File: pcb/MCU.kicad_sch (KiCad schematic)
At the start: 48 parts, among them J3 Conn_ST_STDC14, J4 Micro_SD_Card, SW1 SW_BLUE, SW2 SW_BLACK, U7 STM32U595ZJTx, Y2 16MHz

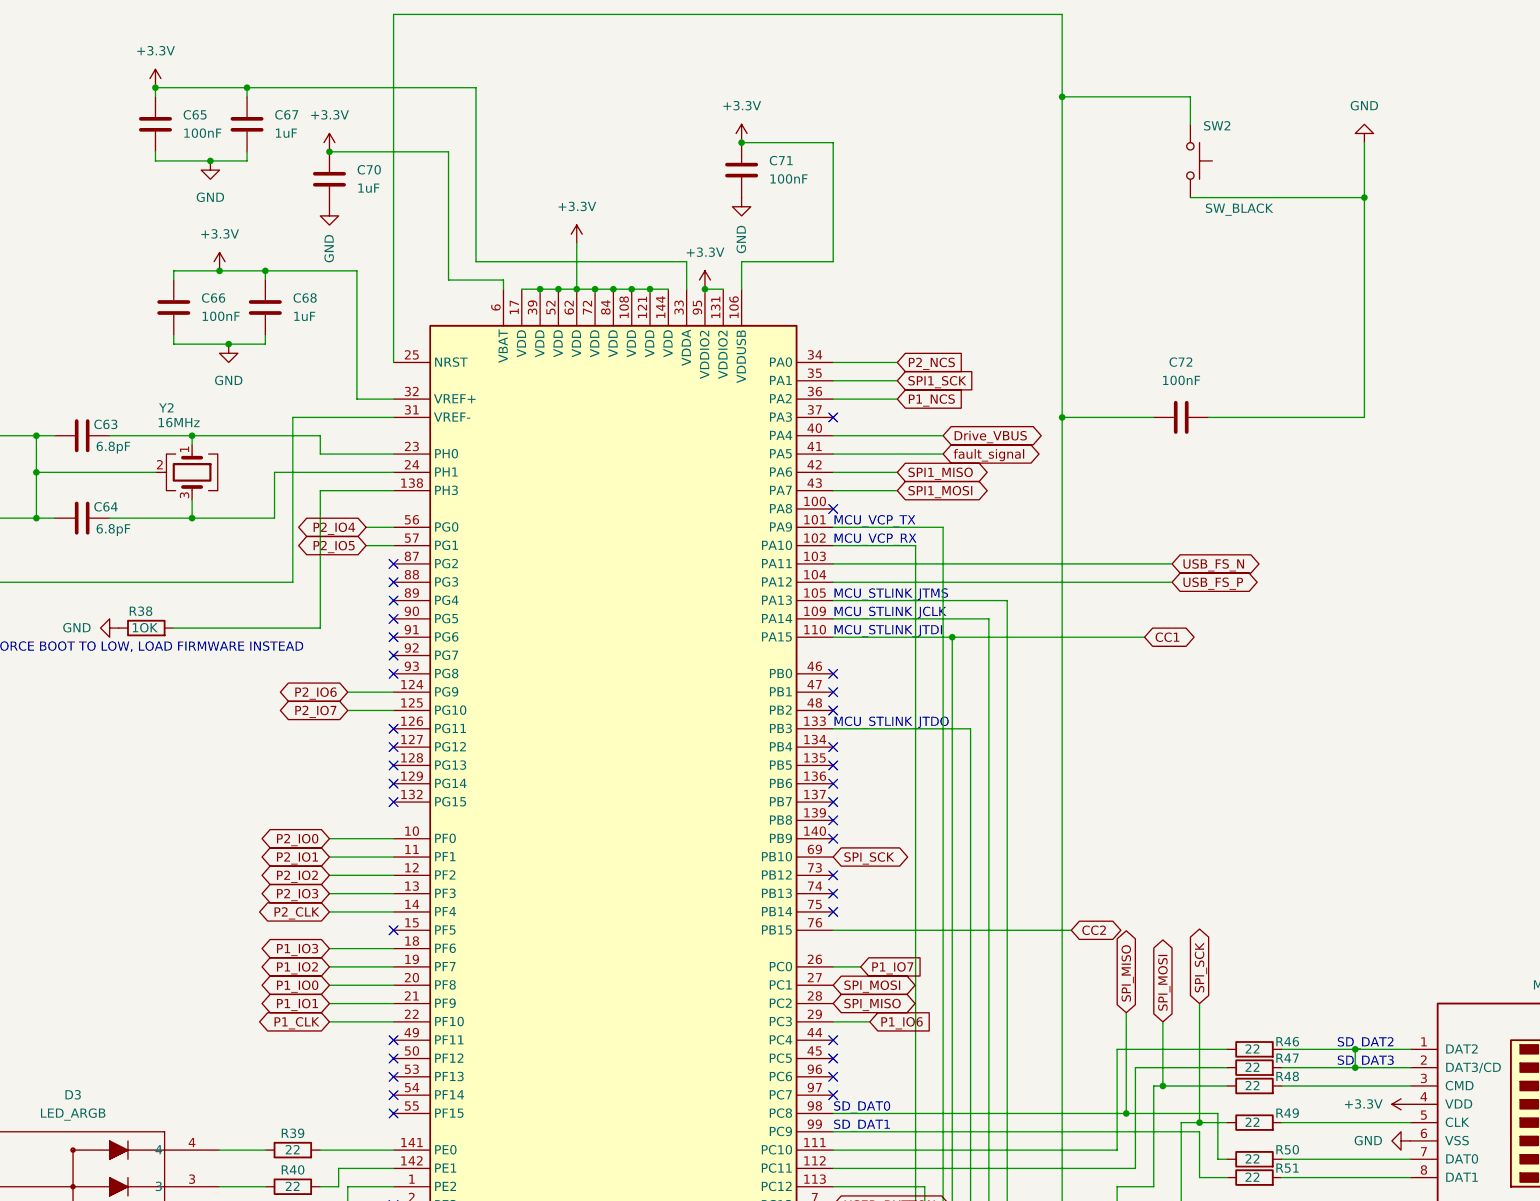
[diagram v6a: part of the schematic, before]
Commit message: pcb: mcu, sd card, jtag layout
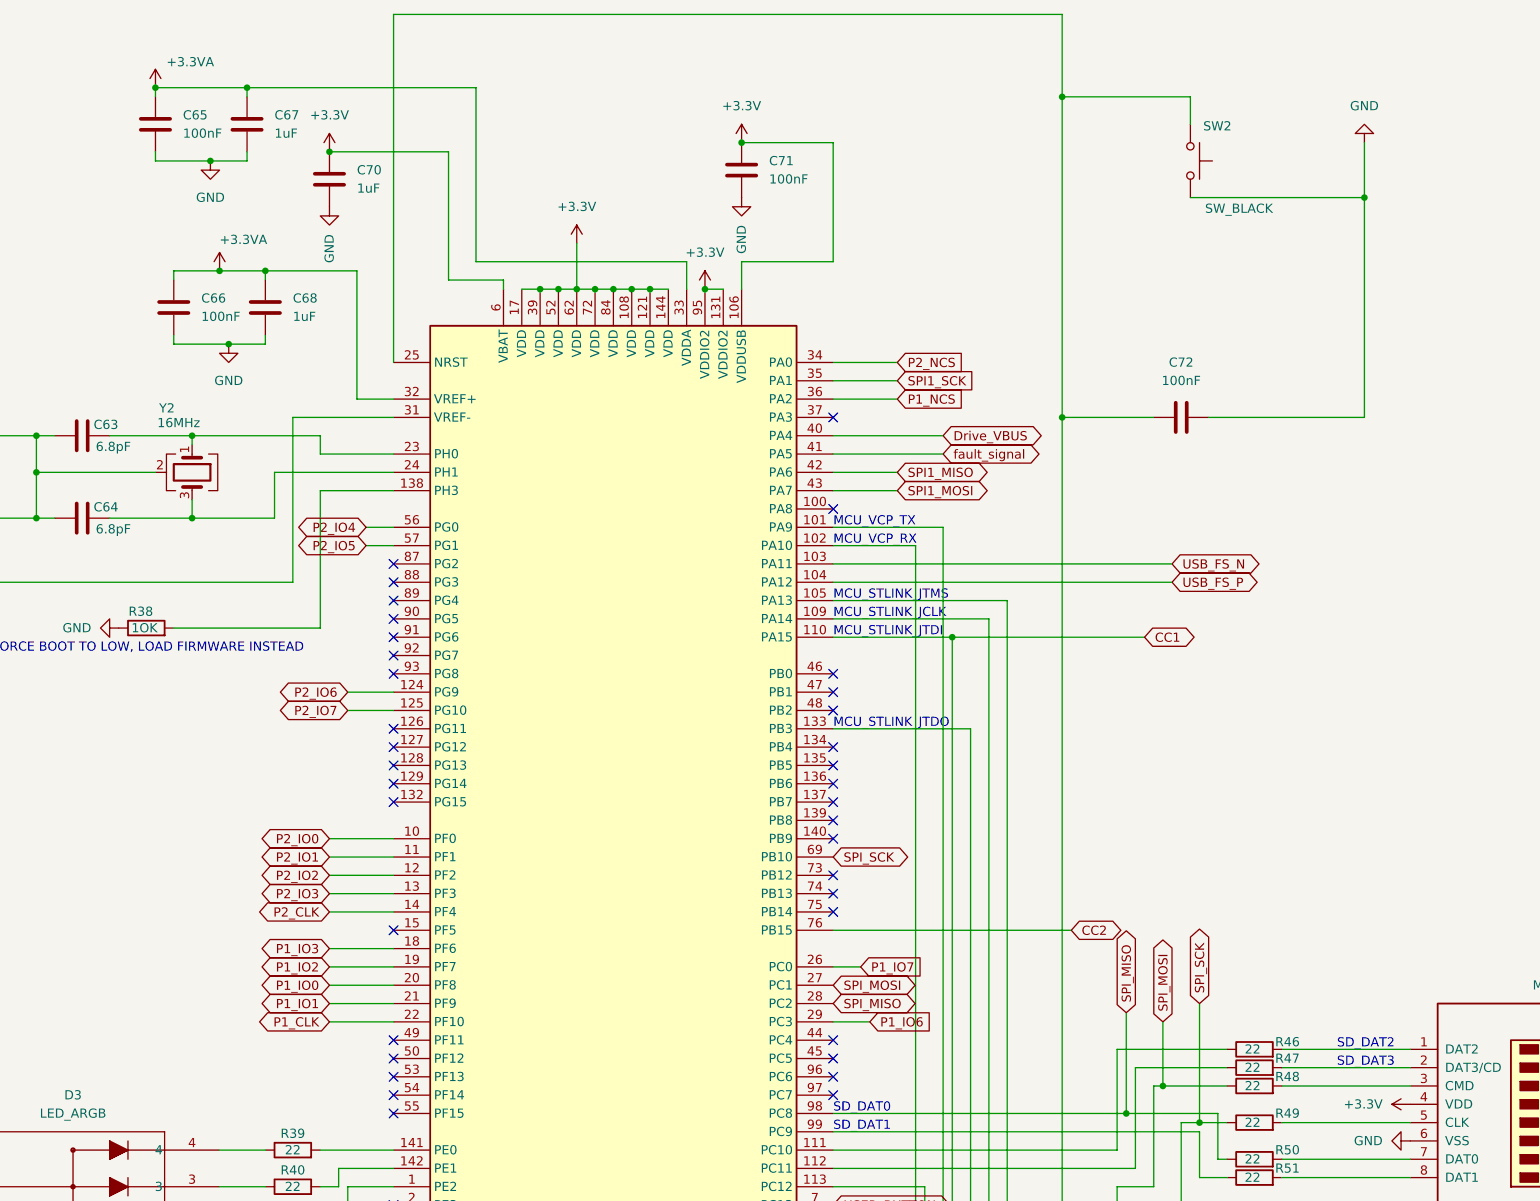
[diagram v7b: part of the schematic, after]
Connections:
- net +3.3V: no longer C65.1, C66.1, C67.1, C68.1, U7.32 (VREF+), U7.33 (VDDA)
- net at J4.1 (DAT2), R46.2: no longer J4.2 (DAT3/CD), R47.2
- new net: J4.2 (DAT3/CD), R47.2
- new net +3.3VA: C65.1, C66.1, C67.1, C68.1, U7.32 (VREF+), U7.33 (VDDA)
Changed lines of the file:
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@@
 	)
 	(junction
-		(at 289.56 166.37)
-		(diameter 0)
-		(color 0 0 0 0)
-	)
-	(junction
 		(at 320.04 217.17)
 		(diameter 0)
@@
 	)
 	(junction
-		(at 289.56 163.83)
-		(diameter 0)
-		(color 0 0 0 0)
-	)
-	(junction
 		(at 35.56 166.37)
 		(diameter 0)
@@
 	(wire
 		(pts
-			(xy 289.56 163.83) (xy 297.18 163.83)
+			(xy 279.4 163.83) (xy 297.18 163.83)
 		)
 		(stroke
@@
 	(wire
 		(pts
-			(xy 279.4 163.83) (xy 289.56 163.83)
-		)
-		(stroke
-			(width 0)
-			(type default)
-		)
-	)
-	(wire
-		(pts
 			(xy 139.7 220.98) (xy 139.7 224.79)
 		)
@@
 	(wire
 		(pts
-			(xy 289.56 163.83) (xy 289.56 166.37)
-		)
-		(stroke
-			(width 0)
-			(type default)
-		)
-	)
-	(wire
-		(pts
 			(xy 142.24 99.06) (xy 78.74 99.06)
 		)
@@
 		(in_pos_files yes)
 		(dnp no)
-		(fields_autoplaced yes)
 		(property "Reference" "#PWR056"
 			(at 132.08 59.69 0)
@@
 			)
 		)
-		(property "Value" "+3.3V"
-			(at 132.08 50.8 0)
+		(property "Value" "+3.3VA"
+			(at 132.08 51.562 0)
 			(show_name no)
 			(do_not_autoplace no)
@@
 					(size 1.27 1.27)
 				)
+				(justify left)
 			)
 		)
@@
 		(in_pos_files yes)
 		(dnp no)
-		(fields_autoplaced yes)
 		(property "Reference" "#PWR054"
 			(at 123.19 34.29 0)
@@
 			)
 		)
-		(property "Value" "+3.3V"
-			(at 123.19 25.4 0)
+		(property "Value" "+3.3VA"
+			(at 124.714 26.924 0)
 			(show_name no)
 			(do_not_autoplace no)
@@
 					(size 1.27 1.27)
 				)
+				(justify left)
 			)
 		)

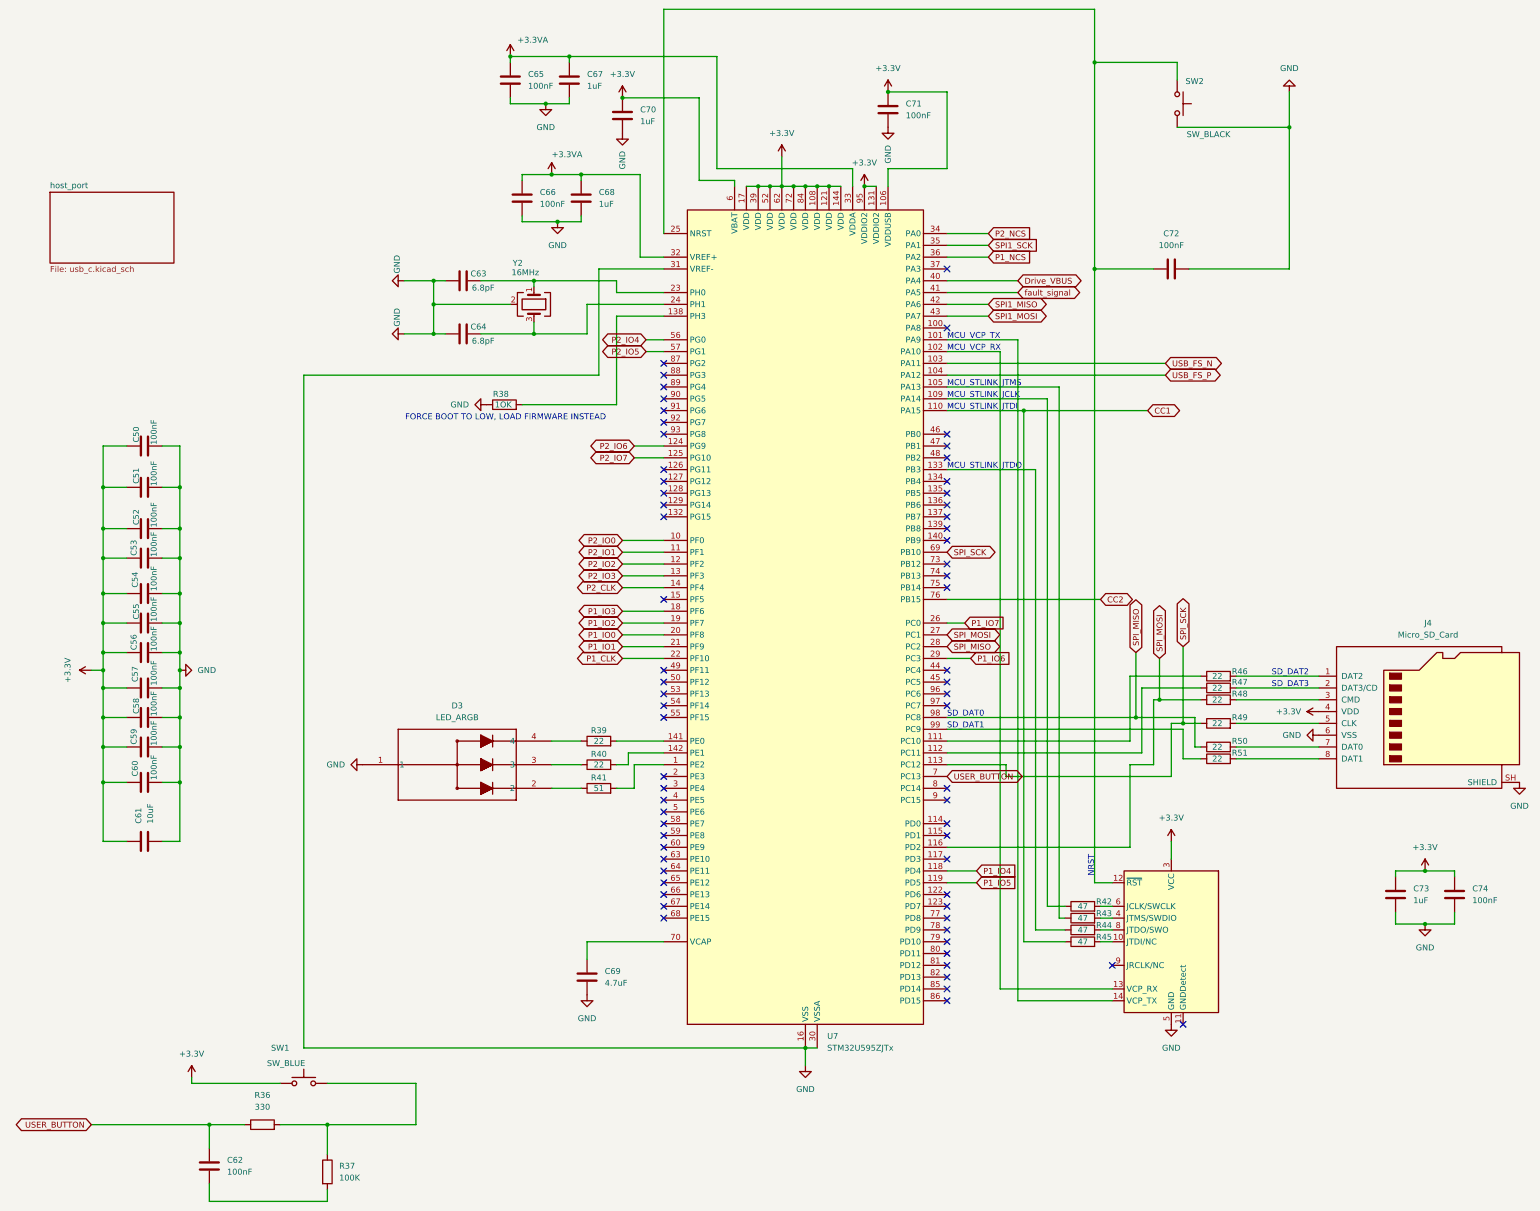
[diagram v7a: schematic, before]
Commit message: pcb: address feedback
- make rgb565 resistor ladder
- add 1v0 diode
- clean up pwr flags
- remove unused mcu-sd spi
- use labels in mcu
- fix broken rgb diode
- connect usblc pin 5 to vbus
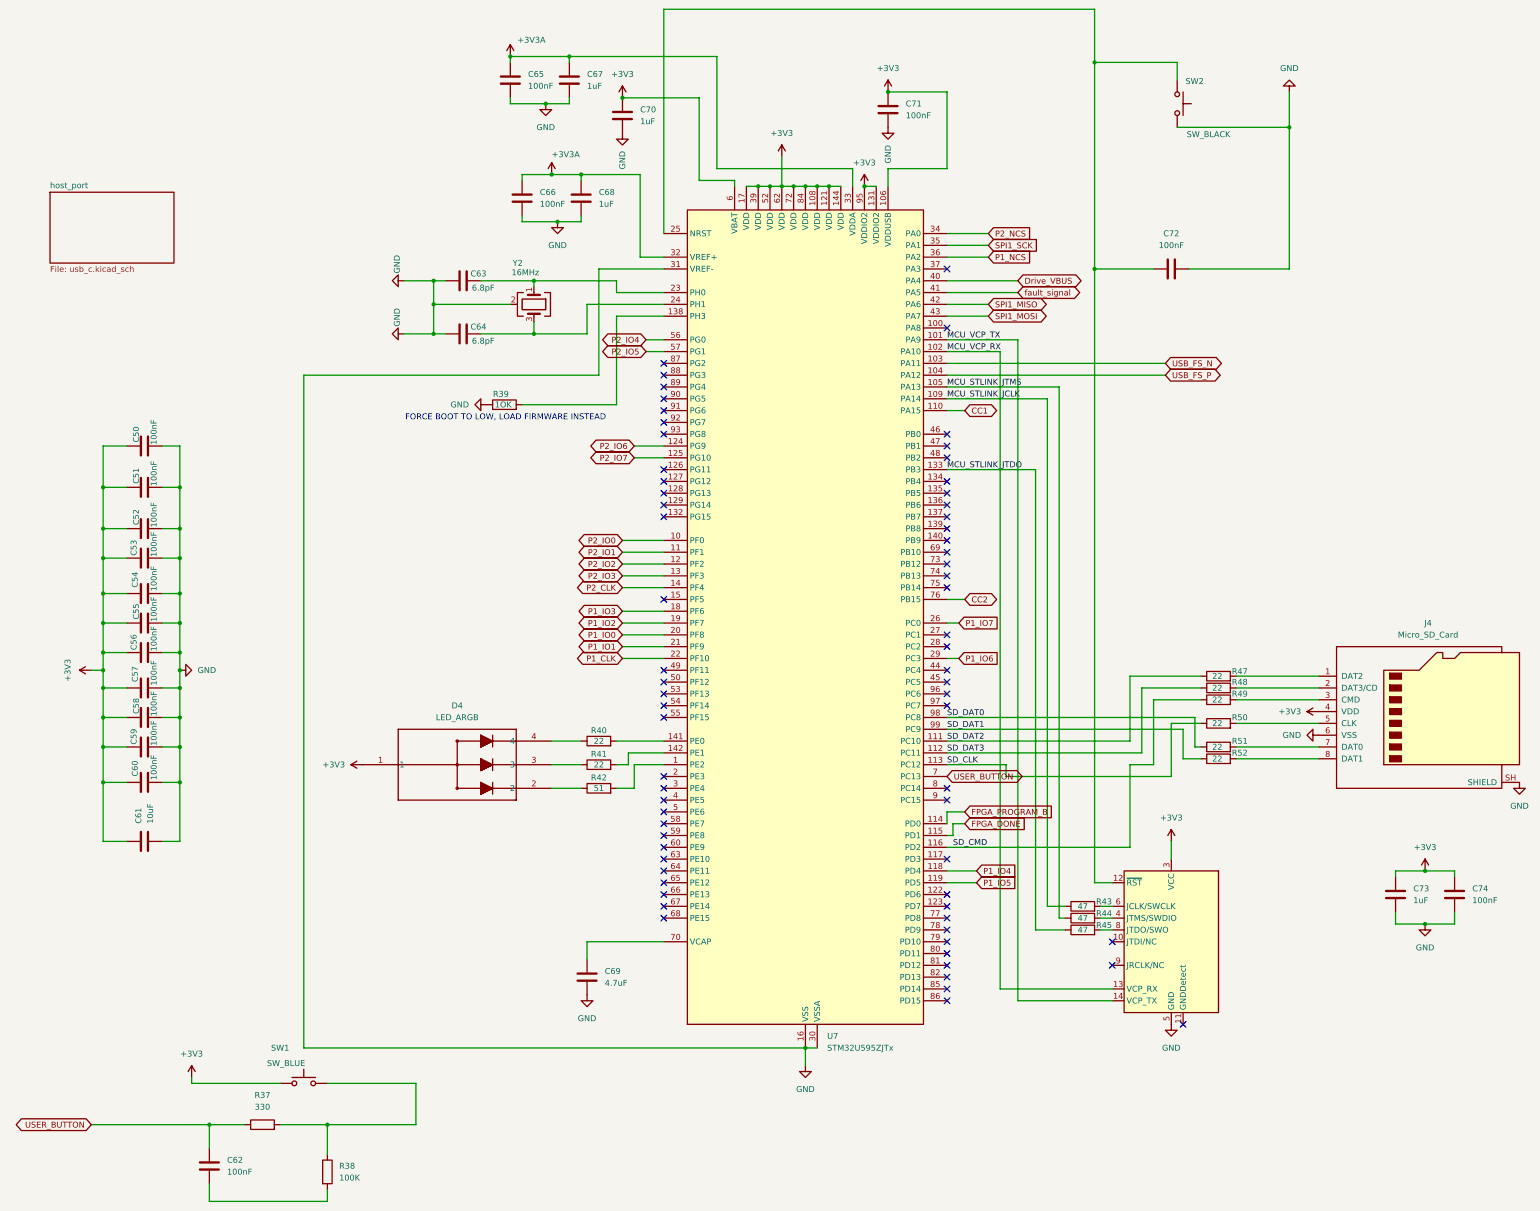
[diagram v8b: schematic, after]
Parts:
- removed R45: 47, Resistor_SMD:R_0805_2012Metric_Pad1.20x1.40mm_HandSolder, symbol Device:R
- renumbered D3 to D4, R36 to R37, R37 to R38, R38 to R39, R39 to R40, R40 to R41, R41 to R42, R42 to R43, R43 to R44, R44 to R45, R46 to R47, R47 to R48, R48 to R49, R49 to R50, R50 to R51, R51 to R52
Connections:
- net GND: no longer D4.1
- net MCU_STLINK_JTDO: now reaches R45.1, U7.133 (PB3)
- net MCU_STLINK_JCLK: now reaches R43.1, U7.109 (PA14)
- net SD_DAT1: now reaches R52.1, U7.99 (PC9)
- net SD_DAT3: now reaches R48.1, U7.112 (PC11)
- net MCU_VCP_RX: now reaches J3.13 (VCP_RX), U7.102 (PA10)
- net MCU_VCP_TX: now reaches J3.14 (VCP_TX), U7.101 (PA9)
- net MCU_STLINK_JTMS: now reaches R44.1, U7.105 (PA13)
- net SD_DAT2: now reaches R47.1, U7.111 (PC10)
- net FPGA_PROGRAM_B: now reaches U7.114 (PD0)
- net FPGA_DONE: now reaches U7.115 (PD1)
- net +3.3V renamed +3V3
- net +3V3: now also D4.1
- net +3.3VA renamed +3V3A
- net SPI_MISO renamed SD_DAT0
- net SD_DAT0: no longer U7.28 (PC2)
- net SPI_MOSI renamed SD_CMD
- net SD_CMD: no longer U7.27 (PC1)
- net SPI_SCK renamed SD_CLK
- net SD_CLK: no longer U7.69 (PB10)
- no-connect marks 66 -> 68
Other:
- note removed: "MCU_STLINK_JCLK"
- note removed: "MCU_STLINK_JTDI"
- note removed: "MCU_STLINK_JTDO"
- note removed: "MCU_STLINK_JTMS"
- note removed: "MCU_VCP_RX"
- note removed: "MCU_VCP_TX"
- note removed: "NRST"
- note removed: "SD_DAT0"
- note removed: "SD_DAT1"
- note removed: "SD_DAT2"
- note removed: "SD_DAT3"
